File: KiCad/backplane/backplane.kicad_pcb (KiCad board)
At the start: 2 copper layers, 160 x 100.1 mm, 38 parts, among them J1 Barrel_Jack_Switch, J10 slot side B, J11 slot side A, J12 slot side B, J13 slot side A, J14 slot side B, J15 slot side A, J16 slot side B, J2 USB_C_Receptacle, J3 slot side A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

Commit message: Changed USB C receptable
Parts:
- removed J2: USB_C_Receptacle, Connector_USB:USB_C_Receptacle_Amphenol_12401548E4-2A
- removed REF** (x6): MountingHole_3.2mm_M3, MountingHole:MountingHole_3.2mm_M3
- added USB1: HRO-TYPE-C-31-M-12, Mini8086:HRO-TYPE-C-31-M-12, F.Cu at (219.2, 79.1)
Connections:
- R1 pad 1: Net-(J2-PadB5) -> /CC2
- R2 pad 1: Net-(J2-PadA5) -> /CC1
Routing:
- net /CC1: track 0.00 -> 23.7 mm
- net /CC2: track 0.00 -> 15.4 mm
- net Net-(J2-PadB5): track 11.8 -> 0.00 mm
- net Net-(J2-PadA5): track 3.16 -> 0.00 mm
- net Net-(Q1-Pad1): track 43.2 -> 43.8 mm
- net /POW_SW: track 67.1 -> 67.6 mm
- net /VBUS: track 29.1 -> 29.6 mm, vias 2 -> 0
- net GND: vias 42 -> 43

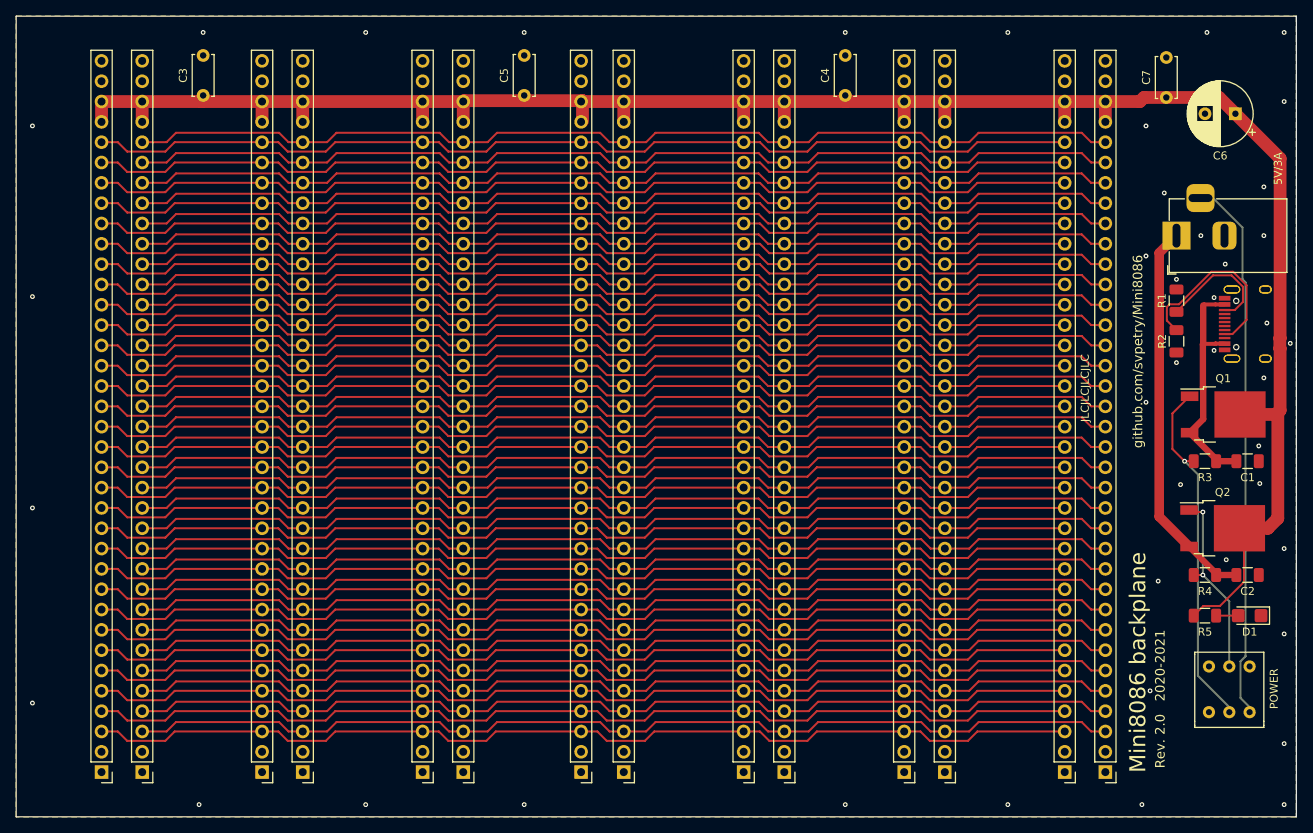
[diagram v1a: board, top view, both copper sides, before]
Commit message: Fixed backplaneV2 bugs
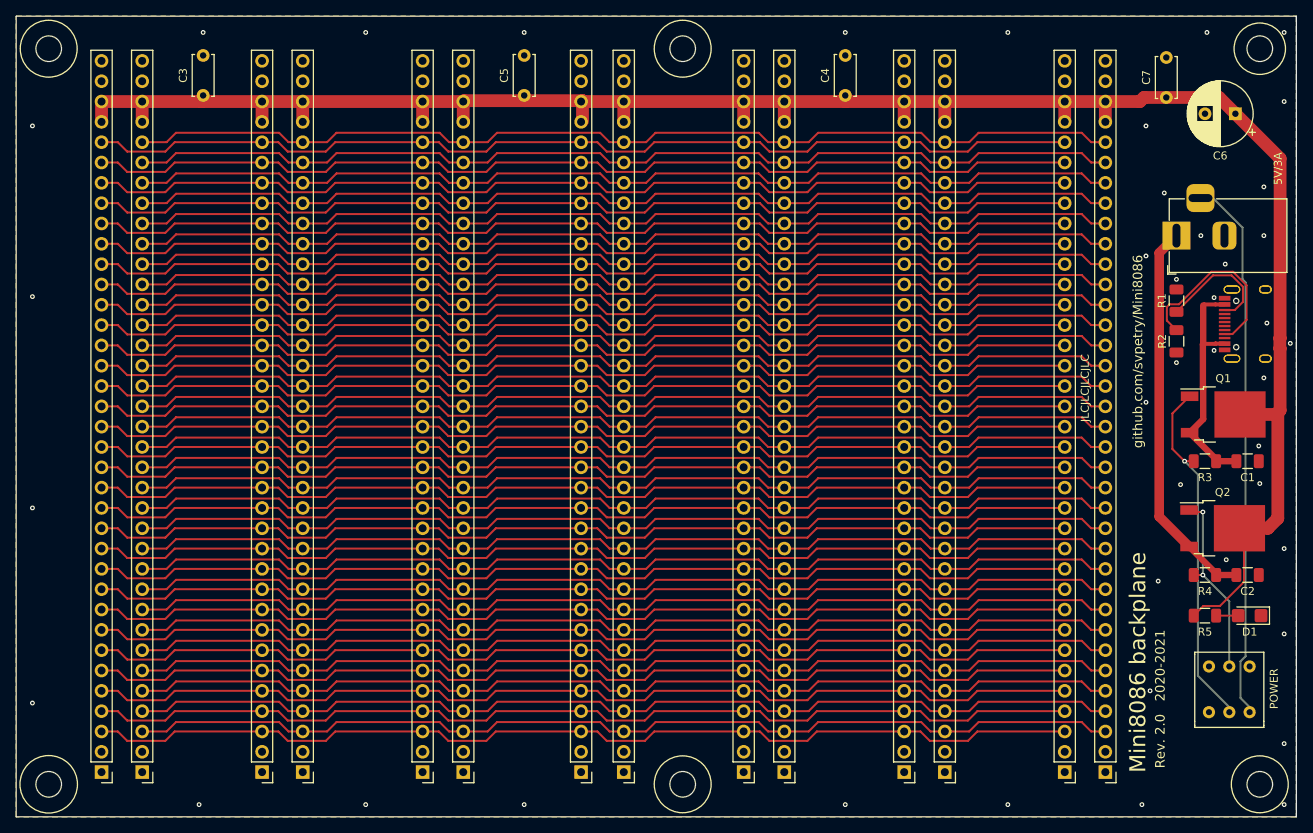
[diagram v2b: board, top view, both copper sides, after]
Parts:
- added REF**: MountingHole_3.2mm_M3_DIN965, MountingHole:MountingHole_3.2mm_M3_DIN965, F.Cu at (215.9, 136.7)
- added REF**: MountingHole_3.2mm_M3_DIN965, MountingHole:MountingHole_3.2mm_M3_DIN965, F.Cu at (215.9, 44.7)
- added REF**: MountingHole_3.2mm_M3_DIN965, MountingHole:MountingHole_3.2mm_M3_DIN965, F.Cu at (143.8, 136.7)
- added REF**: MountingHole_3.2mm_M3_DIN965, MountingHole:MountingHole_3.2mm_M3_DIN965, F.Cu at (143.8, 44.7)
- added REF**: MountingHole_3.2mm_M3_DIN965, MountingHole:MountingHole_3.2mm_M3_DIN965, F.Cu at (64.5, 136.7)
- added REF**: MountingHole_3.2mm_M3_DIN965, MountingHole:MountingHole_3.2mm_M3_DIN965, F.Cu at (64.5, 44.7)

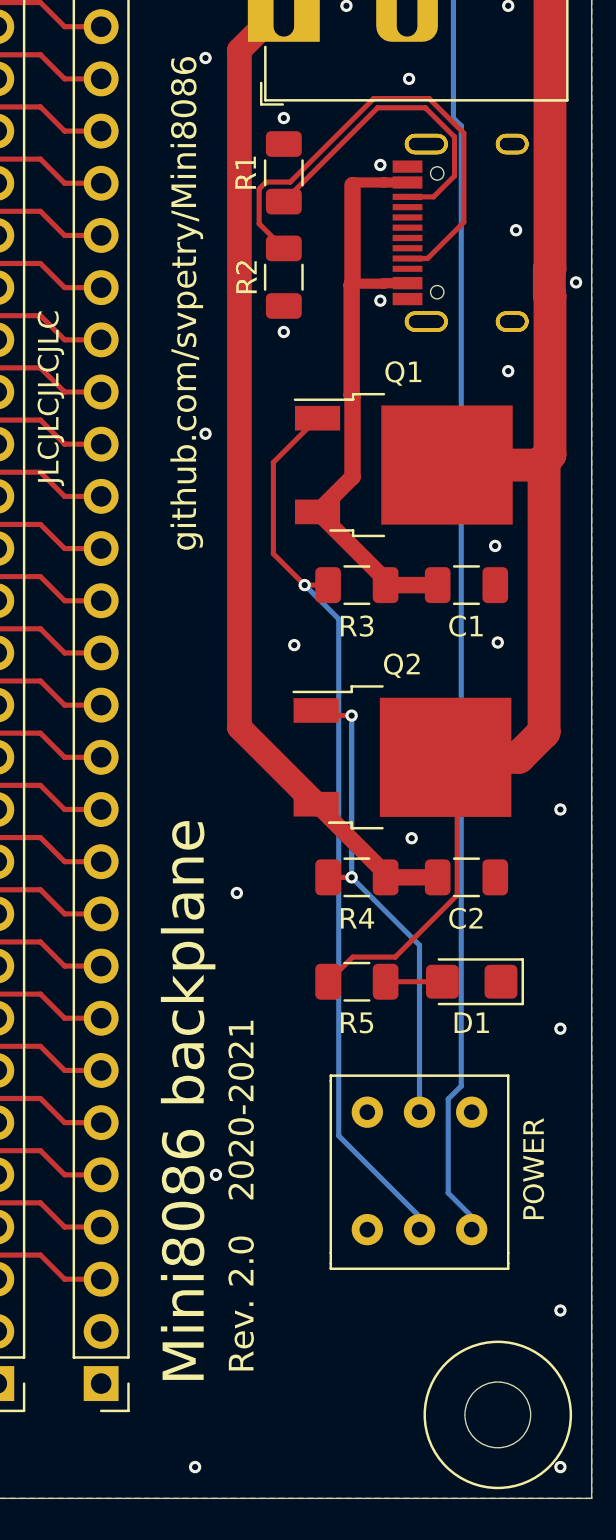
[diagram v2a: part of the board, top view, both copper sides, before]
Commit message: Updated KiCad versioning information in schematics. Fixed button wrong pinout in backplane. Added missing files to git.
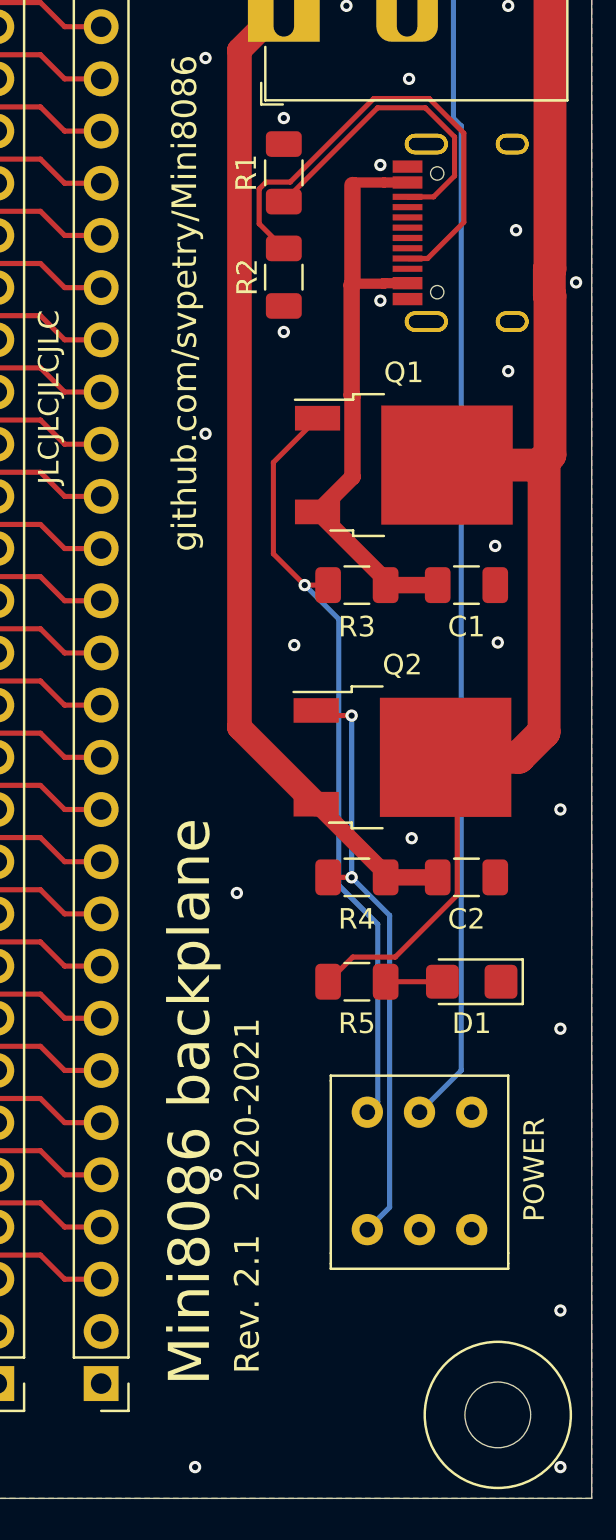
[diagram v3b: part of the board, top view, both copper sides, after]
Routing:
- net Net-(Q1-Pad1): track 43.8 -> 38.1 mm
- net Net-(Q2-Pad1): track 23.8 -> 29.4 mm
- net /POW_SW: track 67.6 -> 62.6 mm
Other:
- board text added: "Rev. 2.1 2020-2021"
- board text removed: "Rev. 2.0 2020-2021"
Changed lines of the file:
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@@
     (thickness 1.6)
     (drawings 25)
-    (tracks 1970)
+    (tracks 1971)
     (zones 0)
     (modules 38)
@@
     (0 F.Cu signal)
     (31 B.Cu signal)
-    (32 B.Adhes user)
+    (32 B.Adhes user hide)
     (33 F.Adhes user hide)
     (34 B.Paste user hide)
-    (35 F.Paste user)
-    (36 B.SilkS user)
+    (35 F.Paste user hide)
+    (36 B.SilkS user hide)
     (37 F.SilkS user)
-    (38 B.Mask user)
-    (39 F.Mask user)
+    (38 B.Mask user hide)
+    (39 F.Mask user hide)
     (40 Dwgs.User user)
     (41 Cmts.User user hide)
@@
     (44 Edge.Cuts user)
     (45 Margin user hide)
-    (46 B.CrtYd user hide)
-    (47 F.CrtYd user hide)
+    (46 B.CrtYd user)
+    (47 F.CrtYd user)
     (48 B.Fab user hide)
-    (49 F.Fab user hide)
+    (49 F.Fab user)
   )
   (setup
@@
     (add_net VCC)
   )
+  (module Mini8086:Button (layer F.Cu)
+    (at 212.09 124.46 90)
+    (fp_text reference SW1 (at 0.635 -5.08 90) (layer F.SilkS) hide
+      (effects (font (size 1 1) (thickness 0.15)))
+    )
+    (fp_text value POWER (at 0 5.08 90) (layer F.Fab)
+      (effects (font (size 1 1) (thickness 0.15)))
+    )
+    (fp_line (start 3.81 3.81) (end 3.175 3.81) (layer F.Fab) (width 0.12))
+    (fp_line (start 3.175 -3.81) (end 3.81 -3.81) (layer F.Fab) (width 0.12))
+    (fp_line (start -4.445 -3.81) (end 3.175 -3.81) (layer F.Fab) (width 0.12))
+    (fp_line (start 3.81 -3.81) (end 3.81 3.81) (layer F.Fab) (width 0.12))
+    (fp_line (start 3.175 3.81) (end -4.445 3.81) (layer F.Fab) (width 0.12))
+    (fp_line (start -4.445 3.81) (end -4.445 -3.81) (layer F.Fab) (width 0.12))
+    (pad 1 thru_hole circle (at 2.54 2.54 90) (size 1.524 1.524) (drill 0.762) (layers *.Cu *.Mask)
+      (net 70 "Net-(SW1-Pad1)"))
+    (pad 3 thru_hole circle (at 2.54 0 90) (size 1.524 1.524) (drill 0.762) (layers *.Cu *.Mask)
+      (net 6 /POW_SW))
+    (pad 2 thru_hole circle (at 2.54 -2.54 90) (size 1.524 1.524) (drill 0.762) (layers *.Cu *.Mask)
+      (net 67 "Net-(Q1-Pad1)"))
+    (pad 4 thru_hole circle (at -3.175 2.54 90) (size 1.524 1.524) (drill 0.762) (layers *.Cu *.Mask)
+      (net 69 "Net-(SW1-Pad4)"))
+    (pad 6 thru_hole circle (at -3.175 0 90) (size 1.524 1.524) (drill 0.762) (layers *.Cu *.Mask)
+      (net 2 GND))
+    (pad 5 thru_hole circle (at -3.175 -2.54 180) (size 1.524 1.524) (drill 0.762) (layers *.Cu *.Mask)
+      (net 68 "Net-(Q2-Pad1)"))
+  )
   (module MountingHole:MountingHole_3.2mm_M3_DIN965 (layer F.Cu)
     (at 215.9 136.652)
@@
       (effects (font (size 1 1) (thickness 0.15)))
     )
+    (fp_circle (center 0 0) (end 2.8 0) (layer Cmts.User) (width 0.15))
+    (fp_circle (center 0 0) (end 3.05 0) (layer F.CrtYd) (width 0.05))
     (fp_text user %R (at 0.3 0) (layer F.Fab)
       (effects (font (size 1 1) (thickness 0.15)))
     )
-    (fp_circle (center 0 0) (end 2.8 0) (layer Cmts.User) (width 0.15))
-    (fp_circle (center 0 0) (end 3.05 0) (layer F.CrtYd) (width 0.05))
     (pad 1 np_thru_hole circle (at 0 0) (size 3.2 3.2) (drill 3.2) (layers *.Cu *.Mask))
   )
@@
       (effects (font (size 1 1) (thickness 0.15)))
     )
+    (fp_circle (center 0 0) (end 2.8 0) (layer Cmts.User) (width 0.15))
+    (fp_circle (center 0 0) (end 3.05 0) (layer F.CrtYd) (width 0.05))
     (fp_text user %R (at 0.3 0) (layer F.Fab)
       (effects (font (size 1 1) (thickness 0.15)))
     )
-    (fp_circle (center 0 0) (end 2.8 0) (layer Cmts.User) (width 0.15))
-    (fp_circle (center 0 0) (end 3.05 0) (layer F.CrtYd) (width 0.05))
     (pad 1 np_thru_hole circle (at 0 0) (size 3.2 3.2) (drill 3.2) (layers *.Cu *.Mask))
   )
@@
       (net 2 GND))
   )
-  (module Mini8086:Button (layer F.Cu)
-    (at 212.09 124.46 90)
-    (fp_text reference SW1 (at 0.635 -5.08 90) (layer F.SilkS) hide
-      (effects (font (size 1 1) (thickness 0.15)))
-    )
-    (fp_text value POWER (at 0 5.08 90) (layer F.Fab)
-      (effects (font (size 1 1) (thickness 0.15)))
-    )
-    (fp_line (start -4.445 3.81) (end -4.445 -3.81) (layer F.Fab) (width 0.12))
-    (fp_line (start 3.175 3.81) (end -4.445 3.81) (layer F.Fab) (width 0.12))
-    (fp_line (start 3.81 -3.81) (end 3.81 3.81) (layer F.Fab) (width 0.12))
-    (fp_line (start -4.445 -3.81) (end 3.175 -3.81) (layer F.Fab) (width 0.12))
-    (fp_line (start 3.175 -3.81) (end 3.81 -3.81) (layer F.Fab) (width 0.12))
-    (fp_line (start 3.81 3.81) (end 3.175 3.81) (layer F.Fab) (width 0.12))
-    (pad 6 thru_hole circle (at 2.54 2.54 90) (size 1.524 1.524) (drill 0.762) (layers *.Cu *.Mask)
-      (net 2 GND))
-    (pad 5 thru_hole circle (at 2.54 0 90) (size 1.524 1.524) (drill 0.762) (layers *.Cu *.Mask)
-      (net 68 "Net-(Q2-Pad1)"))
-    (pad 4 thru_hole circle (at 2.54 -2.54 90) (size 1.524 1.524) (drill 0.762) (layers *.Cu *.Mask)
-      (net 69 "Net-(SW1-Pad4)"))
-    (pad 3 thru_hole circle (at -3.175 2.54 90) (size 1.524 1.524) (drill 0.762) (layers *.Cu *.Mask)
-      (net 6 /POW_SW))
-    (pad 2 thru_hole circle (at -3.175 0 90) (size 1.524 1.524) (drill 0.762) (layers *.Cu *.Mask)
-      (net 67 "Net-(Q1-Pad1)"))
-    (pad 1 thru_hole circle (at -3.175 -2.54 90) (size 1.524 1.524) (drill 0.762) (layers *.Cu *.Mask)
-      (net 70 "Net-(SW1-Pad1)"))
-  )
   (module Connector_PinHeader_2.54mm:PinHeader_1x36_P2.54mm_Vertical (layer F.Cu)
     (at 191.516 135.128 180)
@@
     (effects (font (size 1 1) (thickness 0.15)))
   )
-  (gr_text "Rev. 2.0   2020-2021" (at 203.454 125.984 90) (layer F.SilkS)
+  (gr_text "Rev. 2.1   2020-2021" (at 203.708 125.984 90) (layer F.SilkS)
     (effects (font (size 1.2 1.2) (thickness 0.2)))
   )
-  (gr_text "Mini8086 backplane" (at 200.66 121.412 90) (layer F.SilkS)
+  (gr_text "Mini8086 backplane" (at 200.914 121.412 90) (layer F.SilkS)
     (effects (font (size 2 2) (thickness 0.4)))
   )
@@
   (segment (start 218.409999 80.909999) (end 218.44 80.879998) (width 1.6) (layer F.Cu) (net 4))
   (segment (start 210.442 115.57) (end 213.205 115.57) (width 0.25) (layer F.Cu) (net 5))
-  (segment (start 213.741 73.533) (end 213.741 67.056704) (width 0.25) (layer B.Cu) (net 6))
-  (segment (start 213.487 125.857) (end 213.487 121.285) (width 0.25) (layer B.Cu) (net 6))
   (segment (start 210.056296 63.372) (end 208.486 63.372) (width 0.25) (layer B.Cu) (net 6))
-  (segment (start 214.122 120.65) (end 214.122 73.914) (width 0.25) (layer B.Cu) (net 6))
-  (segment (start 213.741 67.056704) (end 210.056296 63.372) (width 0.25) (layer B.Cu) (net 6))
-  (segment (start 214.63 127) (end 213.487 125.857) (width 0.25) (layer B.Cu) (net 6))
+  (segment (start 214.122 119.888) (end 214.122 73.914) (width 0.25) (layer B.Cu) (net 6))
+  (segment (start 213.741 73.533) (end 213.741 67.056704) (width 0.25) (layer B.Cu) (net 6))
+  (segment (start 212.09 121.92) (end 214.122 119.888) (width 0.25) (layer B.Cu) (net 6))
   (segment (start 214.122 73.914) (end 213.741 73.533) (width 0.25) (layer B.Cu) (net 6))
-  (segment (start 213.487 121.285) (end 214.122 120.65) (width 0.25) (layer B.Cu) (net 6))
+  (segment (start 213.741 67.056704) (end 210.056296 63.372) (width 0.25) (layer B.Cu) (net 6))
   (segment (start 79.248 56.388) (end 76.2 56.388) (width 0.25) (layer F.Cu) (net 7))
   (segment (start 94.488 56.388) (end 93.312999 55.212999) (width 0.25) (layer F.Cu) (net 7))
@@
   (segment (start 179.418999 131.223001) (end 174.657001 131.223001) (width 0.25) (layer F.Cu) (net 66))
   (segment (start 191.516 130.048) (end 180.594 130.048) (width 0.25) (layer F.Cu) (net 66))
-  (via (at 206.502 96.266) (size 0.6) (drill 0.3) (layers F.Cu B.Cu) (net 67))
   (segment (start 206.502 96.266) (end 207.642 96.266) (width 0.25) (layer F.Cu) (net 67))
-  (segment (start 208.162999 123.072999) (end 208.162999 97.926999) (width 0.25) (layer B.Cu) (net 67))
-  (segment (start 208.162999 97.926999) (end 206.502 96.266) (width 0.25) (layer B.Cu) (net 67))
-  (segment (start 212.09 127) (end 208.162999 123.072999) (width 0.25) (layer B.Cu) (net 67))
   (segment (start 204.978 90.294) (end 207.128 88.144) (width 0.25) (layer F.Cu) (net 67))
   (segment (start 206.502 96.266) (end 204.978 94.742) (width 0.25) (layer F.Cu) (net 67))
   (segment (start 204.978 94.742) (end 204.978 90.294) (width 0.25) (layer F.Cu) (net 67))
+  (via (at 206.502 96.266) (size 0.6) (drill 0.3) (layers F.Cu B.Cu) (net 67))
+  (segment (start 210.058 112.776) (end 210.058 121.412) (width 0.25) (layer B.Cu) (net 67))
+  (segment (start 208.162999 110.880999) (end 210.058 112.776) (width 0.25) (layer B.Cu) (net 67))
+  (segment (start 206.502 96.266) (end 208.162999 97.926999) (width 0.25) (layer B.Cu) (net 67))
+  (segment (start 210.058 121.412) (end 209.55 121.92) (width 0.25) (layer B.Cu) (net 67))
+  (segment (start 208.162999 97.926999) (end 208.162999 110.880999) (width 0.25) (layer B.Cu) (net 67))
   (segment (start 208.668999 110.609001) (end 208.788 110.49) (width 0.25) (layer B.Cu) (net 68))
   (via (at 208.788 110.49) (size 0.6) (drill 0.3) (layers F.Cu B.Cu) (net 68))
@@
   (segment (start 207.308 102.616) (end 207.06 102.368) (width 0.25) (layer F.Cu) (net 68))
   (segment (start 208.788 102.616) (end 207.308 102.616) (width 0.25) (layer F.Cu) (net 68))
-  (segment (start 212.09 113.792) (end 208.788 110.49) (width 0.25) (layer B.Cu) (net 68))
-  (segment (start 212.09 121.92) (end 212.09 113.792) (width 0.25) (layer B.Cu) (net 68))
+  (segment (start 210.637001 112.339001) (end 208.788 110.49) (width 0.25) (layer B.Cu) (net 68))
+  (segment (start 210.637001 126.547999) (end 210.637001 112.339001) (width 0.25) (layer B.Cu) (net 68))
+  (segment (start 209.55 127.635) (end 210.637001 126.547999) (width 0.25) (layer B.Cu) (net 68))
   (segment (start 210.051001 73.034999) (end 205.486 77.6) (width 0.25) (layer F.Cu) (net 77))
   (segment (start 212.372739 73.034999) (end 210.051001 73.034999) (width 0.25) (layer F.Cu) (net 77))

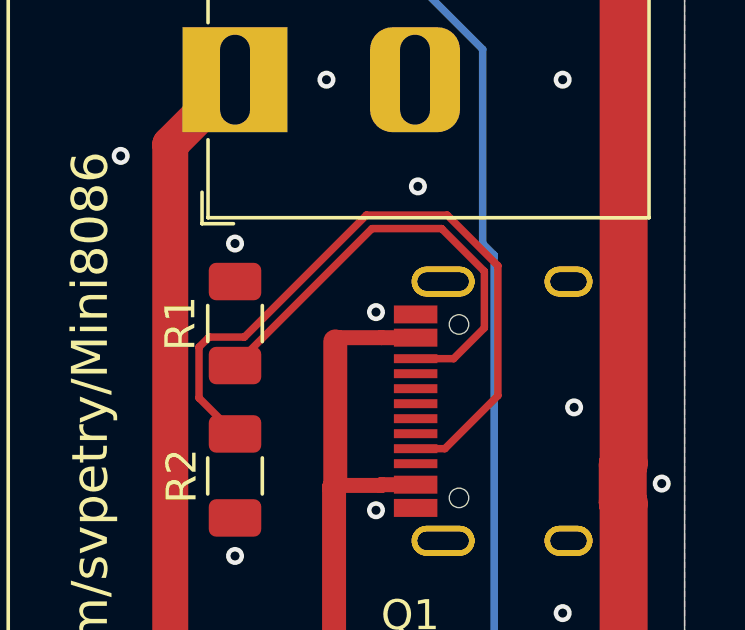
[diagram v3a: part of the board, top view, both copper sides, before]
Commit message: Migration from KiCad 5 to KiCad 7
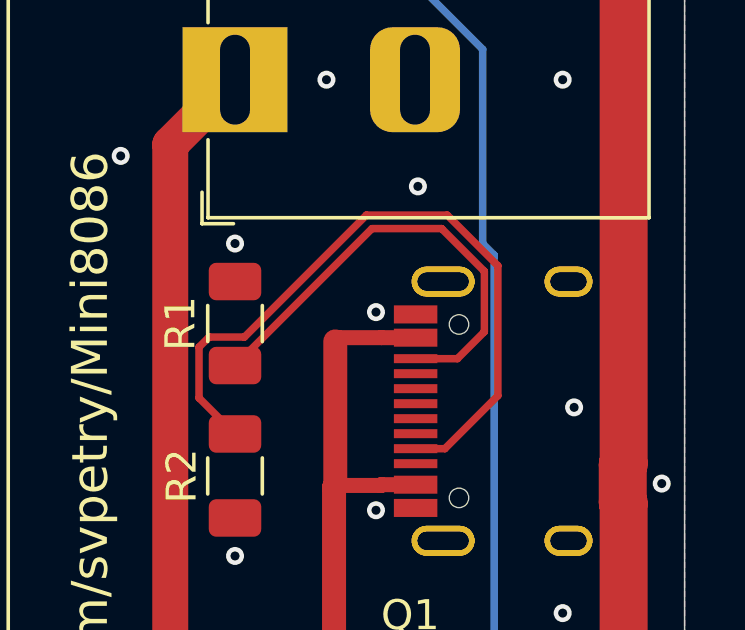
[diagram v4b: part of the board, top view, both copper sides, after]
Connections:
- SW1 pad 1: Net-(SW1-Pad1) -> unconnected-(SW1-A-Pad1)
- SW1 pad 4: Net-(SW1-Pad4) -> unconnected-(SW1-A-Pad4)
- USB1 pad 3: Net-(USB1-Pad3) -> unconnected-(USB1-SBU2-Pad3)
- USB1 pad 5: Net-(USB1-Pad5) -> unconnected-(USB1-DN2-Pad5)
- USB1 pad 6: Net-(USB1-Pad6) -> unconnected-(USB1-DP1-Pad6)
- USB1 pad 7: Net-(USB1-Pad7) -> unconnected-(USB1-DN1-Pad7)
- USB1 pad 8: Net-(USB1-Pad8) -> unconnected-(USB1-DP2-Pad8)
- USB1 pad 9: Net-(USB1-Pad9) -> unconnected-(USB1-SBU1-Pad9)
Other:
- net class Default removed
